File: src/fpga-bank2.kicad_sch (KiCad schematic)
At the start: 21 parts

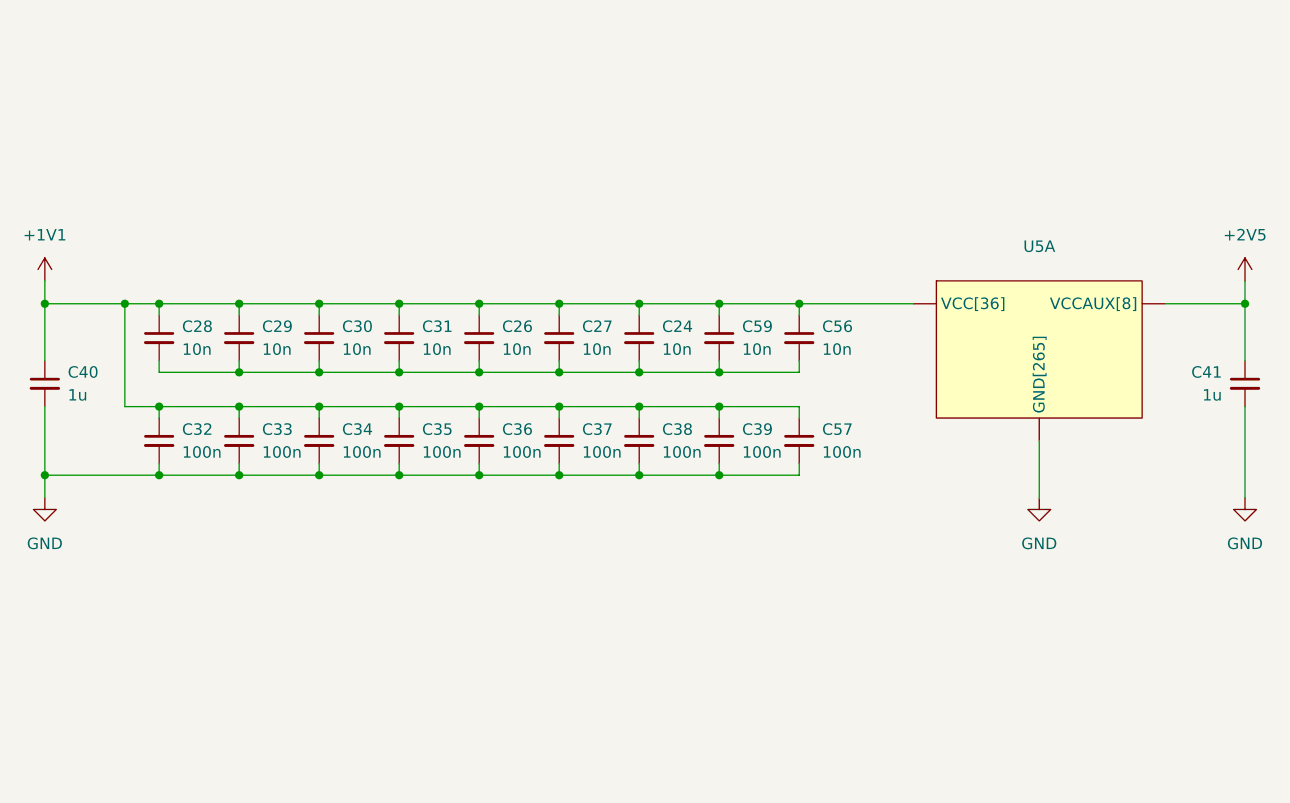
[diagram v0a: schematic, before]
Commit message: Adds more FPGA IO banks
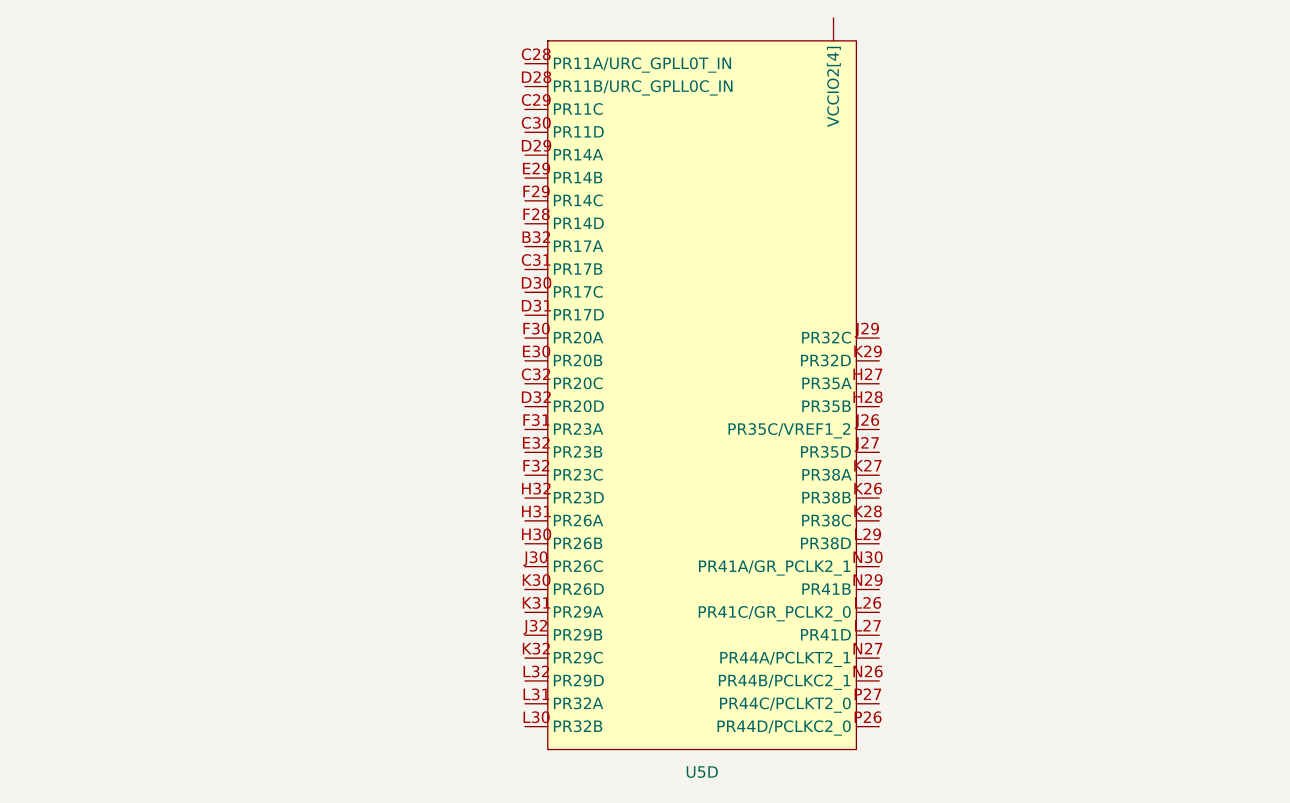
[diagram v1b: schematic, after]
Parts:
- removed C24, C26, C27, C28, C29, C30, C31, C56, C59: 10n, symbol Device:C_Small
- removed C32, C33, C34, C35, C36, C37, C38, C39, C57: 100n, symbol Device:C_Small
- removed C40, C41: 1u, symbol Device:C_Small
- removed U5: ~, symbol ECAP5-BSOM:LFE5U-85F-*BG756*
- added U5: ~, symbol ECAP5-BSOM:LFE5U-85F-*BG756*
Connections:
- new net VCCIO2: U5. (VCCIO2[4]), U5.M23 (VCCIO2), U5.P23 (VCCIO2), U5.R23 (VCCIO2), U5.T23 (VCCIO2)
